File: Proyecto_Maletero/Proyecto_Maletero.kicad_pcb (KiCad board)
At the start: 2 copper layers, 65.4 x 59.2 mm, 49 parts, among them J1 DE9_Pins, J2 Conn_01x02, J3 Conn_01x02, J4 Conn_01x03, J5 Conn_01x02, J6 DE9_Pins, J7 Conn_01x04, J9 Conn_01x04, K1 FINDER-34.51, Q2 MMBT5550L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

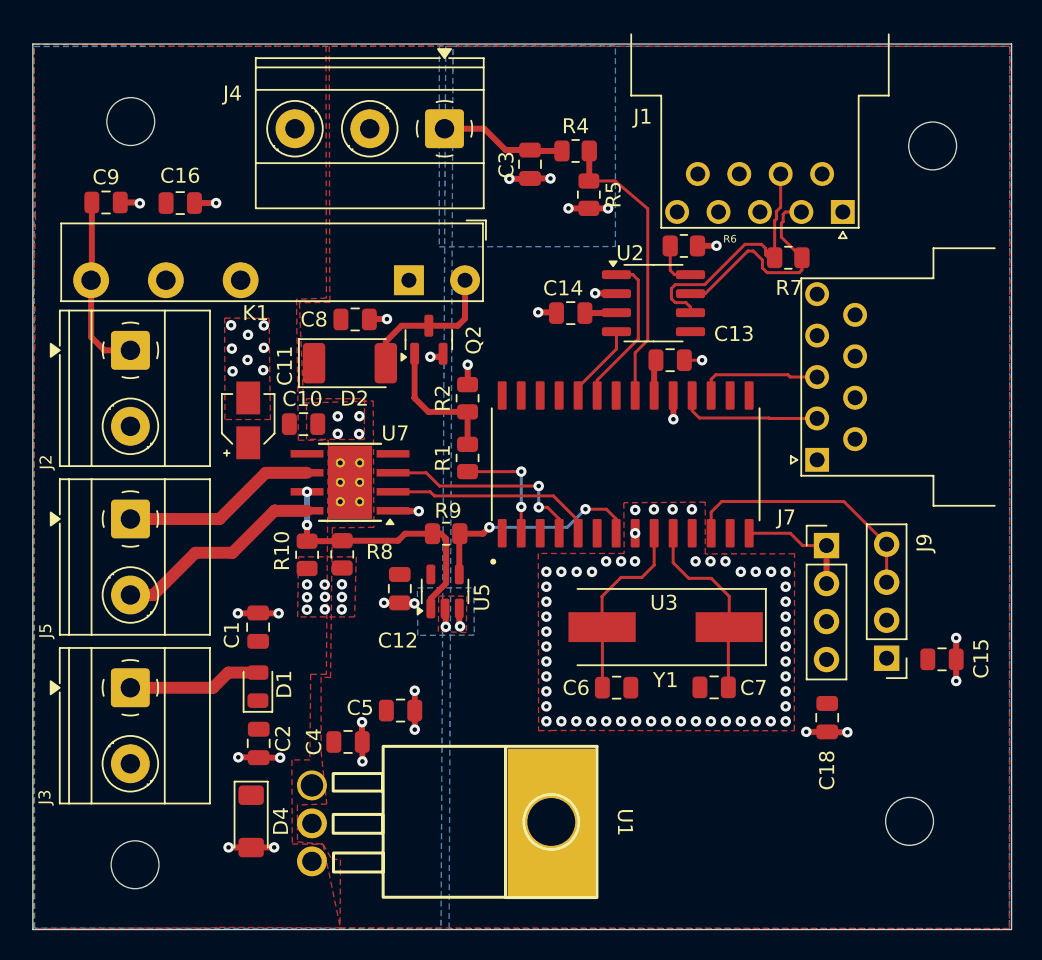
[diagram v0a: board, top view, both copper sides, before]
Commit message: Actualizacion layout
Colocacion idonias de tornillos, simetrias y reduccion de avisos de 8 a 2
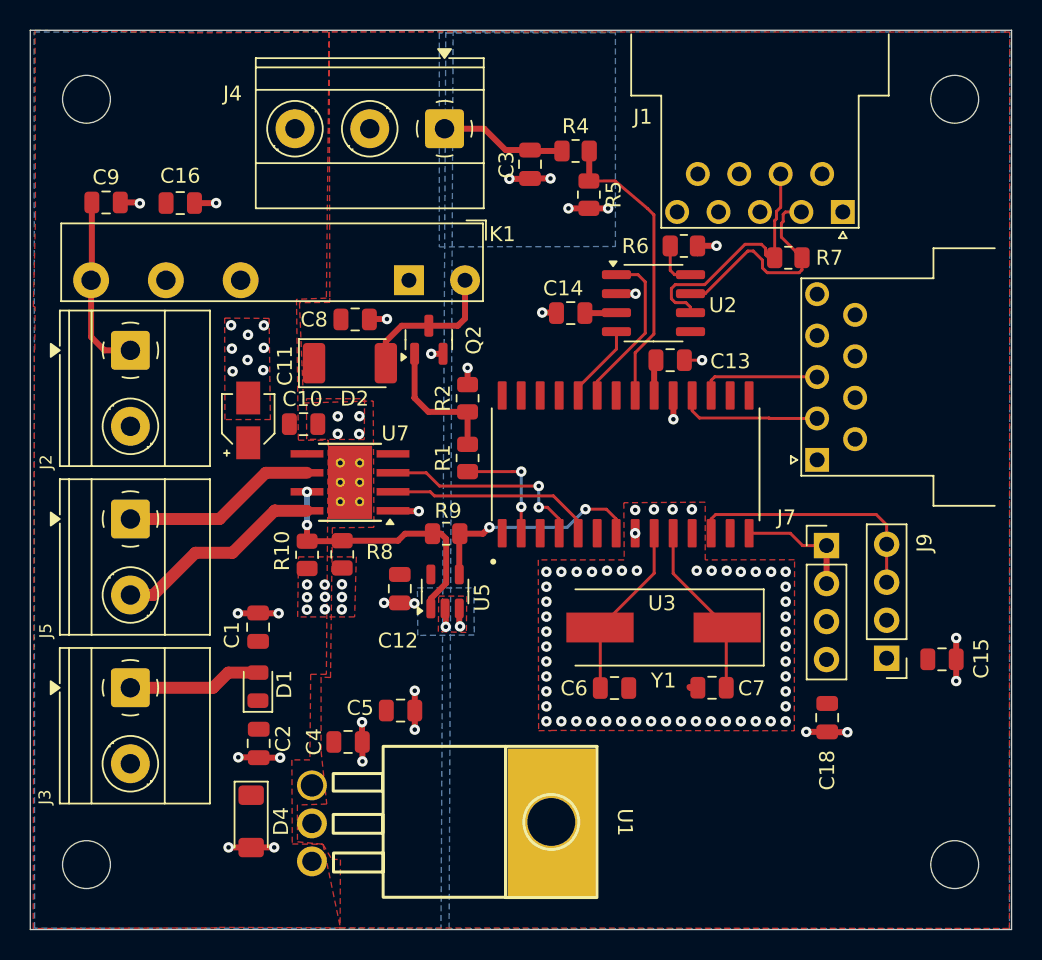
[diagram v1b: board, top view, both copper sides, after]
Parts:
- moved REF** 4.18 mm to (170.0, 138.9)
- moved REF** 3.45 mm to (170.0, 87.7)
- moved REF** 3.31 mm to (112.0, 87.7)
- moved REF** 3.25 mm to (112.0, 138.9)
- moved C6 0.14 mm to (147.3, 127.1)
- moved Y1 0.14 mm to (150.5, 123.0)
- moved C7 0.14 mm to (153.8, 127.1)
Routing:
- net Osc_2: track 12.8 -> 11.9 mm
- net Osc_1: track 12.6 -> 11.9 mm
- net CAN_TX: track 10.7 -> 11.3 mm
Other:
- board size 65.4 x 59.2 mm -> 65.6 x 60.1 mm
- board text added: "17.04.2025"
- board text added: "2.0"
- board text added: "AUTORS"
- board text added: "Eric Trejo Sanchez Eloi Ortega Ortiz"
- board text added: "Proyecto Maletero"

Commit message: Actulizacion Placa
Mover de9
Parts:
- moved J6 0.41 mm to (161.2, 111.8)
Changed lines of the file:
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@@
 	(footprint "Connector_Dsub:DSUB-9_Pins_Horizontal_P2.77x2.54mm_EdgePinOffset9.40mm"
 		(layer "F.Cu")
-		(at 160.799669 111.84 90)
+		(at 161.21 111.785 90)
 		(descr "9-pin D-Sub connector, horizontal/angled (90 deg), THT-mount, pins (male), pitch 2.77x2.54mm, pin-PCB-offset 9.4mm, see https://docs.rs-online.com/02d6/0900766b81585df2.pdf")
 		(tags "9-pin D-Sub connector horizontal angled 90deg THT pins pitch 2.77x2.54mm pin-PCB-offset 9.4mm")
@@
 	)
 	(segment
-		(start 157.62 109.07)
-		(end 160.799669 109.07)
-		(width 0.2)
-		(layer "F.Cu")
-		(net 16)
-	)
-	(segment
-		(start 157.59 109.04)
-		(end 157.62 109.07)
+		(start 161.185 109.04)
+		(end 152.93 109.04)
 		(width 0.2)
 		(layer "F.Cu")
@@
 	)
 	(segment
-		(start 157.59 109.04)
-		(end 152.93 109.04)
+		(start 152.93 109.04)
+		(end 152.445 108.555)
 		(width 0.2)
 		(layer "F.Cu")
@@
 	)
 	(segment
-		(start 152.93 109.04)
-		(end 152.445 108.555)
+		(start 161.21 109.015)
+		(end 161.185 109.04)
 		(width 0.2)
 		(layer "F.Cu")
@@
 	(segment
 		(start 153.715 106.525)
-		(end 153.715 107.535)
+		(end 153.995 106.245)
 		(width 0.2)
 		(layer "F.Cu")
@@
 	)
 	(segment
-		(start 160.783669 106.284)
-		(end 153.956 106.284)
+		(start 153.995 106.245)
+		(end 161.21 106.245)
 		(width 0.2)
 		(layer "F.Cu")
@@
 	)
 	(segment
-		(start 153.956 106.284)
+		(start 153.715 107.535)
 		(end 153.715 106.525)
 		(width 0.2)

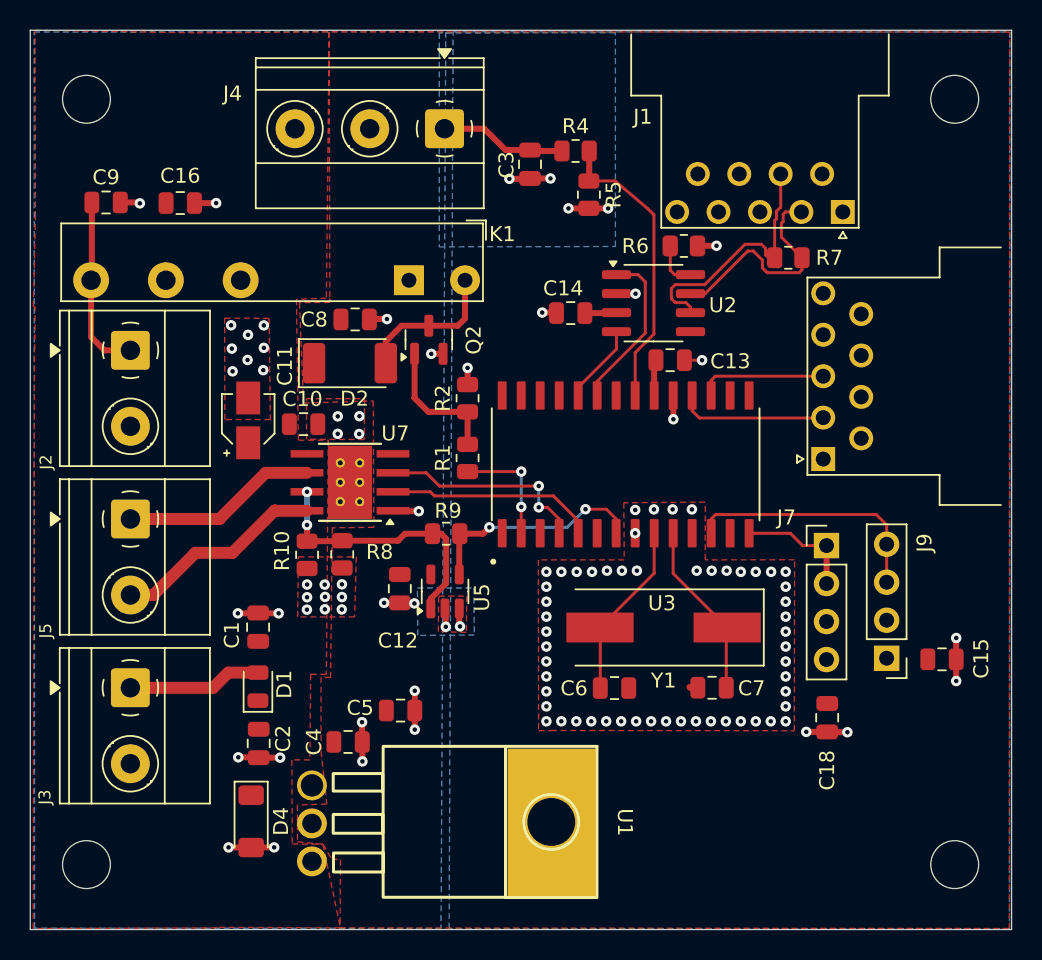
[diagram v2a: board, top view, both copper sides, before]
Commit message: Orden de carpetas, referencia a los autores layout (nosotros)
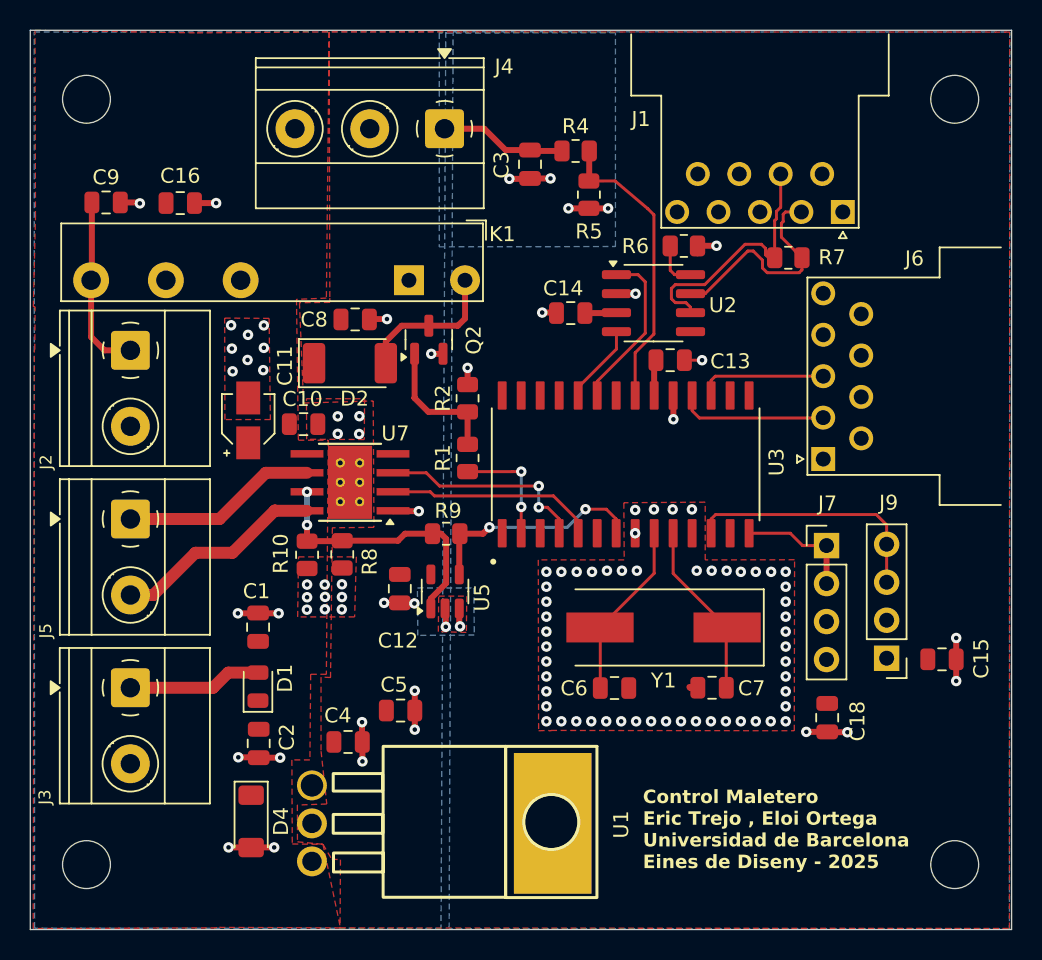
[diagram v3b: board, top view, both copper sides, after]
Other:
- board text added: "Control Maletero Eric Trejo , Eloi Ortega Universidad de Barcelona Eines de Diseny - 2025"
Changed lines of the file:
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@@
 		(tags "resistor")
 		(property "Reference" "R5"
-			(at 0 -1.65 90)
+			(at 2.4638 0 180)
 			(layer "F.SilkS")
 			(effects
@@
 		(at 151.6254 136.144 -90)
 		(property "Reference" "U1"
-			(at -0.074 3.6754 270)
+			(at 0.0762 3.9244 90)
 			(unlocked yes)
 			(layer "F.SilkS")
@@
 		(pad "2" thru_hole rect
 			(at -0.095 8.5975 270)
-			(size 10 6)
-			(drill 3.2
+			(size 9.4 5.2)
+			(drill 3.5
 				(offset 0.095 -0.0975)
 			)
@@
 		(tags "capacitor")
 		(property "Reference" "C3"
-			(at 0.045 1.575 90)
+			(at 0.045 1.905 90)
 			(layer "F.SilkS")
 			(effects
@@
 		(tags "diode")
 		(property "Reference" "D1"
-			(at 0.15 1.76 90)
+			(at 0.5588 1.807 90)
 			(layer "F.SilkS")
 			(effects
@@
 		(tags "capacitor")
 		(property "Reference" "C2"
-			(at -0.325 -1.635 90)
+			(at -0.4218 -1.884 90)
 			(layer "F.SilkS")
 			(effects
@@
 		(tags "resistor")
 		(property "Reference" "R8"
-			(at -0.1575 -2.5 180)
+			(at 0.4859 -1.8362 270)
 			(layer "F.SilkS")
 			(effects
@@
 		(tags "Through hole pin header THT 1x04 2.54mm single row")
 		(property "Reference" "J7"
-			(at -2.68 -1.88 0)
+			(at 0.0632 -2.8128 0)
 			(layer "F.SilkS")
 			(effects
@@
 		(tags "9-pin D-Sub connector horizontal angled 90deg THT pins pitch 2.77x2.54mm pin-PCB-offset 9.4mm")
 		(property "Reference" "J1"
-			(at 13.3712 6.365331 0)
+			(at 13.4982 6.212931 0)
 			(layer "F.SilkS")
 			(effects
@@
 		(tags "THT Terminal Block Phoenix MKDS-1,5-3 pitch 5mm size 15x9.8mm drill 1.3mm pad 2.6mm")
 		(property "Reference" "J4"
-			(at 14.1732 2.3494 0)
+			(at -3.9878 4.1528 0)
 			(layer "F.SilkS")
 			(effects
@@
 		(tags "capacitor")
 		(property "Reference" "C5"
-			(at -2.7 -0.175 0)
+			(at -0.4382 -1.727 0)
 			(layer "F.SilkS")
 			(effects
@@
 		(tags "capacitor")
 		(property "Reference" "C1"
-			(at -0.525 -1.75 90)
+			(at 2.4004 -0.108 180)
 			(layer "F.SilkS")
 			(effects
@@
 		(tags "resistor")
 		(property "Reference" "R10"
-			(at 0.2625 -1.675 90)
+			(at 0.0775 -1.7574 90)
 			(layer "F.SilkS")
 			(effects
@@
 		(tags "9-pin D-Sub connector horizontal angled 90deg THT pins pitch 2.77x2.54mm pin-PCB-offset 9.4mm")
 		(property "Reference" "J6"
-			(at 5.54 -1.8 90)
+			(at 13.4108 6.0998 180)
 			(layer "F.SilkS")
-			(hide yes)
 			(effects
 				(font
@@
 		(tags "resistor")
 		(property "Reference" "R7"
-			(at -2.745 -0.005 180)
+			(at -2.923 0.027 180)
 			(layer "F.SilkS")
 			(effects
@@
 		(tags "capacitor")
 		(property "Reference" "C18"
-			(at -3.52 0 90)
+			(at -0.2364 2.0248 90)
 			(layer "F.SilkS")
 			(effects
@@
 		)
 		(property "Value" "100n"
-			(at 0 1.68 90)
+			(at -0.1094 -1.9122 90)
 			(layer "F.Fab")
 			(effects
@@
 		(at 148 112.14 90)
 		(property "Reference" "U3"
-			(at -9.287 2.425 0)
+			(at 0.1514 10.0896 90)
 			(layer "F.SilkS")
 			(effects
@@
 		(tags "Through hole pin header THT 1x04 2.54mm single row")
 		(property "Reference" "J9"
-			(at -2.53 7.71 90)
+			(at -0.1326 10.3936 180)
 			(layer "F.SilkS")
 			(effects
@@
 		(tags "capacitor")
 		(property "Reference" "C4"
-			(at -2.28 -0.01 90)
+			(at -0.6874 -1.7696 180)
 			(layer "F.SilkS")
 			(effects
@@
 		(layer "Edge.Cuts")
 	)
+	(gr_text "Control Maletero\nEric Trejo , Eloi Ortega\nUniversidad de Barcelona\nEines de Diseny - 2025"
+		(at 149.1488 139.2428 0)
+		(layer "F.SilkS")
+		(effects
+			(font
+				(size 0.9 0.9)
+				(thickness 0.18)
+				(bold yes)
+			)
+			(justify left bottom)
+		)
+	)
 	(gr_text "2.0\n"
